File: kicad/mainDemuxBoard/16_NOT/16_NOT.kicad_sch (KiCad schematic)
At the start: 32 parts, among them Q169 NMOS, Q170 NMOS, Q171 NMOS, Q172 NMOS, Q173 NMOS, Q174 NMOS, Q175 NMOS, Q176 NMOS, Q177 NMOS, Q178 NMOS, Q179 NMOS, Q180 NMOS, Q181 NMOS, Q182 NMOS, Q183 NMOS, Q184 NMOS

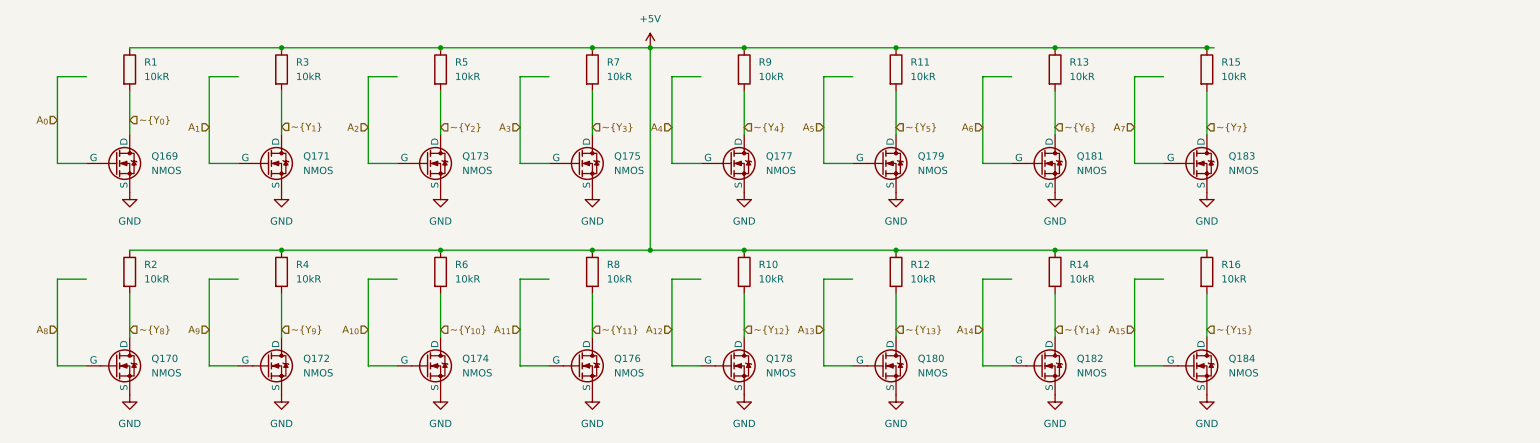
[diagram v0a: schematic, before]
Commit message: update main board schematic
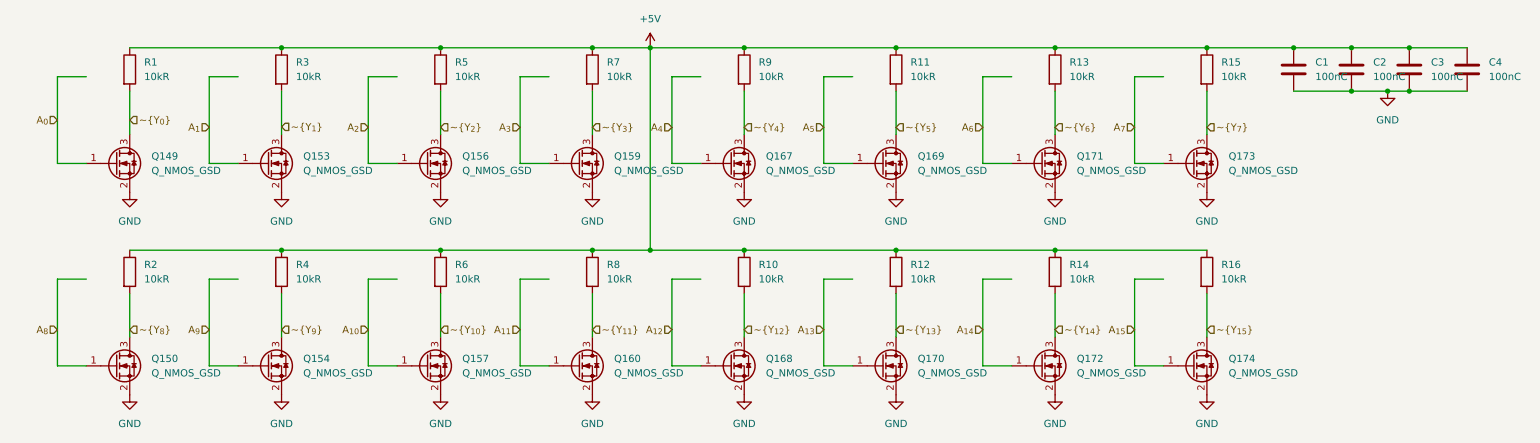
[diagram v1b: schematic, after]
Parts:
- added C1, C2, C3, C4: 100nC, Capacitor_SMD:C_0603_1608Metric, symbol Device:C
- Q149: renamed from Q169; value NMOS -> Q_NMOS_GSD; symbol Simulation_SPICE:NMOS -> Transistor_FET:Q_NMOS_GSD
- Q150: renamed from Q170; value NMOS -> Q_NMOS_GSD; symbol Simulation_SPICE:NMOS -> Transistor_FET:Q_NMOS_GSD
- Q153: renamed from Q171; value NMOS -> Q_NMOS_GSD; symbol Simulation_SPICE:NMOS -> Transistor_FET:Q_NMOS_GSD
- Q154: renamed from Q172; value NMOS -> Q_NMOS_GSD; symbol Simulation_SPICE:NMOS -> Transistor_FET:Q_NMOS_GSD
- Q156: renamed from Q173; value NMOS -> Q_NMOS_GSD; symbol Simulation_SPICE:NMOS -> Transistor_FET:Q_NMOS_GSD
- Q157: renamed from Q174; value NMOS -> Q_NMOS_GSD; symbol Simulation_SPICE:NMOS -> Transistor_FET:Q_NMOS_GSD
- Q159: renamed from Q175; value NMOS -> Q_NMOS_GSD; symbol Simulation_SPICE:NMOS -> Transistor_FET:Q_NMOS_GSD
- Q160: renamed from Q176; value NMOS -> Q_NMOS_GSD; symbol Simulation_SPICE:NMOS -> Transistor_FET:Q_NMOS_GSD
- Q167: renamed from Q177; value NMOS -> Q_NMOS_GSD; symbol Simulation_SPICE:NMOS -> Transistor_FET:Q_NMOS_GSD
- Q168: renamed from Q178; value NMOS -> Q_NMOS_GSD; symbol Simulation_SPICE:NMOS -> Transistor_FET:Q_NMOS_GSD
- Q169: renamed from Q179; value NMOS -> Q_NMOS_GSD; symbol Simulation_SPICE:NMOS -> Transistor_FET:Q_NMOS_GSD
- Q170: renamed from Q180; value NMOS -> Q_NMOS_GSD; symbol Simulation_SPICE:NMOS -> Transistor_FET:Q_NMOS_GSD
- Q171: renamed from Q181; value NMOS -> Q_NMOS_GSD; symbol Simulation_SPICE:NMOS -> Transistor_FET:Q_NMOS_GSD
- Q172: renamed from Q182; value NMOS -> Q_NMOS_GSD; symbol Simulation_SPICE:NMOS -> Transistor_FET:Q_NMOS_GSD
- Q173: renamed from Q183; value NMOS -> Q_NMOS_GSD; symbol Simulation_SPICE:NMOS -> Transistor_FET:Q_NMOS_GSD
- Q174: renamed from Q184; value NMOS -> Q_NMOS_GSD; symbol Simulation_SPICE:NMOS -> Transistor_FET:Q_NMOS_GSD
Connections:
- net +5V: now also C1.1, C2.1, C3.1, C4.1
- net A_{0}: now also Q149.1 (G); no longer Q149.2 (G)
- net A_{10}: now also Q157.1 (G); no longer Q157.2 (G)
- net A_{11}: now also Q160.1 (G); no longer Q160.2 (G)
- net A_{12}: now also Q168.1 (G); no longer Q168.2 (G)
- net A_{13}: now also Q170.1 (G); no longer Q170.2 (G)
- net A_{14}: now also Q172.1 (G); no longer Q172.2 (G)
- net A_{15}: now also Q174.1 (G); no longer Q174.2 (G)
- net A_{1}: now also Q153.1 (G); no longer Q153.2 (G)
- net A_{2}: now also Q156.1 (G); no longer Q156.2 (G)
- net A_{3}: now also Q159.1 (G); no longer Q159.2 (G)
- net A_{4}: now also Q167.1 (G); no longer Q167.2 (G)
- net A_{5}: now also Q169.1 (G); no longer Q169.2 (G)
- net A_{6}: now also Q171.1 (G); no longer Q171.2 (G)
- net A_{7}: now also Q173.1 (G); no longer Q173.2 (G)
- net A_{8}: now also Q150.1 (G); no longer Q150.2 (G)
- net A_{9}: now also Q154.1 (G); no longer Q154.2 (G)
- net GND: now also Q149.2 (S), Q150.2 (S), Q153.2 (S), Q154.2 (S), Q156.2 (S), Q157.2 (S), Q159.2 (S), Q160.2 (S), Q167.2 (S), Q168.2 (S), Q169.2 (S), Q170.2 (S), Q171.2 (S), Q172.2 (S), Q173.2 (S), Q174.2 (S), C1.2, C2.2, C3.2, C4.2; no longer Q149.3 (S), Q150.3 (S), Q153.3 (S), Q154.3 (S), Q156.3 (S), Q157.3 (S), Q159.3 (S), Q160.3 (S), Q167.3 (S), Q168.3 (S), Q169.3 (S), Q170.3 (S), Q171.3 (S), Q172.3 (S), Q173.3 (S), Q174.3 (S)
- net ~{Y_{0}}: now also Q149.3 (D); no longer Q149.1 (D)
- net ~{Y_{10}}: now also Q157.3 (D); no longer Q157.1 (D)
- net ~{Y_{11}}: now also Q160.3 (D); no longer Q160.1 (D)
- net ~{Y_{12}}: now also Q168.3 (D); no longer Q168.1 (D)
- net ~{Y_{13}}: now also Q170.3 (D); no longer Q170.1 (D)
- net ~{Y_{14}}: now also Q172.3 (D); no longer Q172.1 (D)
- net ~{Y_{15}}: now also Q174.3 (D); no longer Q174.1 (D)
- net ~{Y_{1}}: now also Q153.3 (D); no longer Q153.1 (D)
- net ~{Y_{2}}: now also Q156.3 (D); no longer Q156.1 (D)
- net ~{Y_{3}}: now also Q159.3 (D); no longer Q159.1 (D)
- net ~{Y_{4}}: now also Q167.3 (D); no longer Q167.1 (D)
- net ~{Y_{5}}: now also Q169.3 (D); no longer Q169.1 (D)
- net ~{Y_{6}}: now also Q171.3 (D); no longer Q171.1 (D)
- net ~{Y_{7}}: now also Q173.3 (D); no longer Q173.1 (D)
- net ~{Y_{8}}: now also Q150.3 (D); no longer Q150.1 (D)
- net ~{Y_{9}}: now also Q154.3 (D); no longer Q154.1 (D)
